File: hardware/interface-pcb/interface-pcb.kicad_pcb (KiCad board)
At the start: 2 copper layers, 100 x 80 mm, 101 parts, among them J1 Siedle bus Ta/Tb, J2 ext. 5V, Q1 IRFR120N, Q2 BC846B, Q3 BCP56-16, Q4 BCP56-16, Q5 BC846B, SW1 setup, U1 R-78CK5.0-0.5, U2 LM393, U3 ES8311, U4 MCP6002, U5 ESP32 D1 Mini

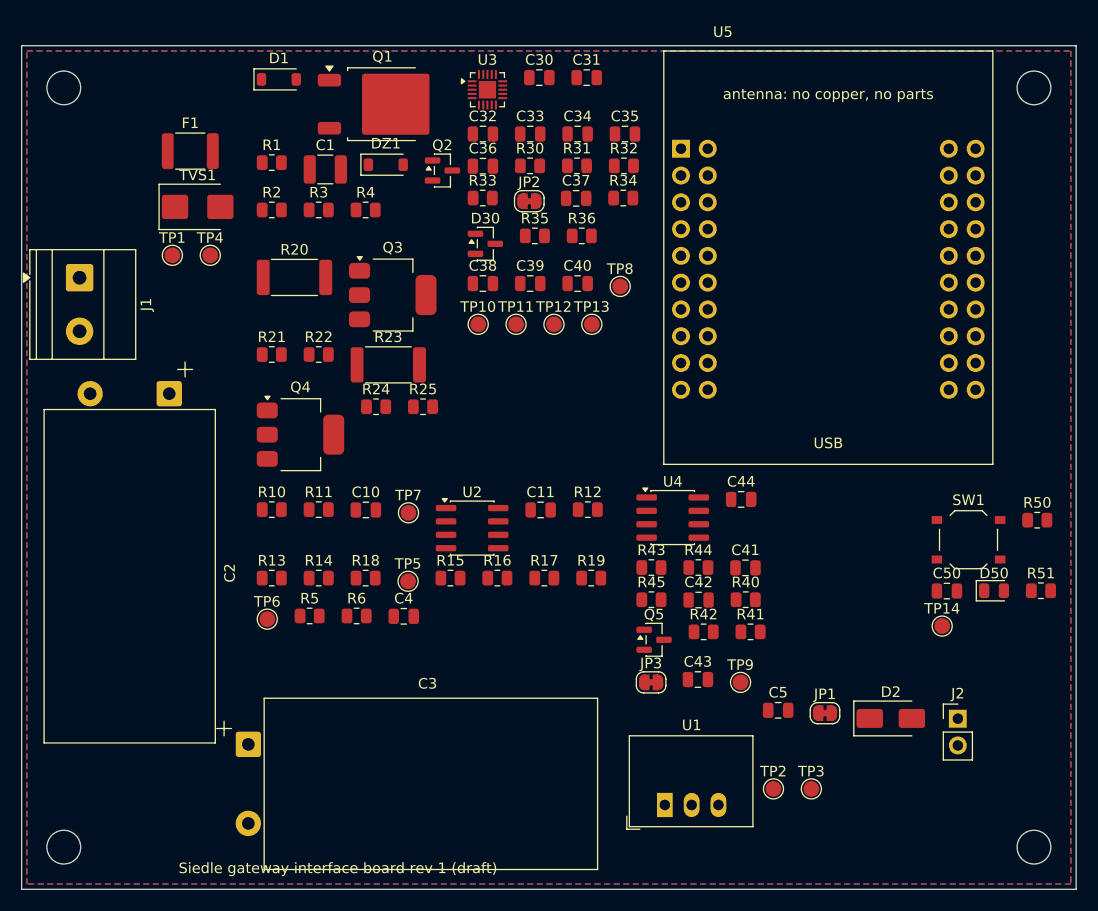
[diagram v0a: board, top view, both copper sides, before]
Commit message: Route the interface board
Routed with Codex: local Freerouting passes, then corrections in
KiCad. The board shrinks to 90 x 75 mm. Audio moves to the lower
middle, away from the antenna and the regulator, which moves to the
right edge.

- Power nets 0.5 mm, pull-down collectors 0.6-0.8 mm, a copper area
  on Q1's drain for the startup heat.
- GND pours on both layers with 63 stitching vias; the ES8311's
  exposed pad reaches its ground pins through short necks, with a
  local 0.15 mm clearance rule for its corner pads
  (interface-pcb.kicad_dru). The board-wide rules get stricter.
- New net classes Ground and Codec; the socket 3D models now sit on
  their pad rows (KiCad's 2 x 10 socket has pin 2 at -2.54 mm).

DRC with refilled zones: no violations, no unconnected items, no
schematic parity issues. PCB.md gets the dimensions for the case.
AGENTS.md records the KiCad scripting pitfalls on macOS, and
tools/kicad-python wraps KiCad's Python with a log.

Co-Authored-By: Claude Opus 5.5 <noreply@anthropic.com>
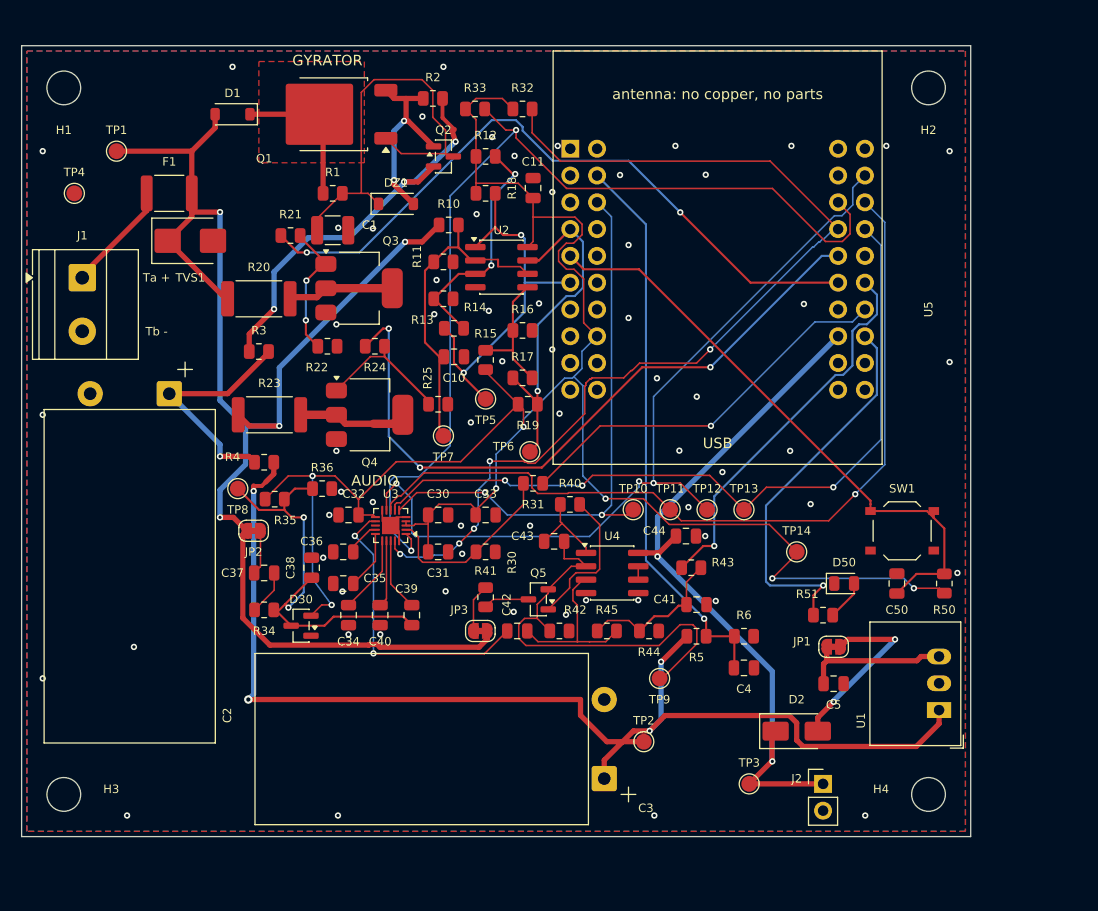
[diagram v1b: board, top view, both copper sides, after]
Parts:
- moved R34 51.8 mm to (73.0, 103.5)
- moved C34 50.5 mm to (81.0, 104.0), turned to -90 degrees
- moved C35 50.3 mm to (80.5, 101.0), turned to 180 degrees
- moved C31 47.1 mm to (89.5, 98.0)
- moved C37 46.2 mm to (73.0, 100.0)
- moved C30 42.6 mm to (89.5, 94.5)
- moved U3 42.3 mm to (85.0, 95.5), turned to 180 degrees
- moved TP8 41.0 mm to (70.5, 92.0)
- moved JP2 40.7 mm to (72.0, 96.0)
- moved D30 40.2 mm to (76.5, 105.0), turned to 180 degrees
- moved C36 38.9 mm to (80.5, 98.0), turned to 180 degrees
- moved C32 38.3 mm to (81.0, 94.5), turned to 180 degrees
- moved R18 38.2 mm to (94.0, 64.0)
- moved R30 36.8 mm to (94.0, 98.0)
- moved R6 36.8 mm to (118.5, 106.0)
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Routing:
- net +3V3: track 0.00 -> 185.0 mm, vias 0 -> 7
- net BUS: track 0.00 -> 133.8 mm, vias 0 -> 4
- net /Bus input and power/VOUT: track 0.00 -> 114.1 mm, vias 0 -> 4
- net I2C_SDA: track 0.00 -> 95.7 mm, vias 0 -> 5
- net I2C_SCL: track 0.00 -> 92.9 mm, vias 0 -> 2
- net I2S_WS: track 0.00 -> 79.1 mm, vias 0 -> 1
- net I2S_DOUT: track 0.00 -> 77.9 mm, vias 0 -> 3
- net I2S_DIN: track 0.00 -> 72.9 mm, vias 0 -> 3
- net +5V: track 0.00 -> 69.6 mm, vias 0 -> 2
- net TX_CARRIER: track 0.00 -> 65.3 mm, vias 0 -> 2
- net TX_BIT: track 0.00 -> 65.3 mm, vias 0 -> 3
- net /BUTTON: track 0.00 -> 57.0 mm
- net I2S_BCLK: track 0.00 -> 54.6 mm, vias 0 -> 2
- net VMON: track 0.00 -> 53.7 mm, vias 0 -> 1
- net /Audio/TX_FB: track 0.00 -> 41.2 mm
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- added copper zone on F.Cu, net /Bus input and power/GYR_D
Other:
- board size 100 x 80 mm -> 90 x 75 mm
- board text added: "AUDIO"
- board text added: "GYRATOR"
- board text added: "SIEDLE GATEWAY / REV 1 DRAFT"
- board text added: "Ta +"
- board text added: "Tb -"
- board text removed: "Siedle gateway interface board rev 1 (draft)"

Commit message: Name the MIC1N net
The redraw wired MIC1N directly, so the Codec net class matched it by
KiCad's pin-derived name, Net-(U3-MIC1N), which changes when U3 or
its pins are renumbered. A label makes it /Audio/MIC1N in the
schematic, the board and the net class pattern.

Co-Authored-By: Claude Opus 5.5 <noreply@anthropic.com>
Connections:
- net Net-(U3-MIC1N) renamed /Audio/MIC1N
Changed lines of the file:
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@@
 			(layers "F.Cu" "F.Mask" "F.Paste")
 			(roundrect_rratio 0.25)
-			(net "Net-(U3-MIC1N)")
+			(net "/Audio/MIC1N")
 		)
 		(pad "2" smd roundrect
@@
 			(layers "F.Cu" "F.Mask" "F.Paste")
 			(roundrect_rratio 0.25)
-			(net "Net-(U3-MIC1N)")
+			(net "/Audio/MIC1N")
 		)
 		(pad "18" smd roundrect
@@
 		(width 0.15)
 		(layer "F.Cu")
-		(net "Net-(U3-MIC1N)")
+		(net "/Audio/MIC1N")
 	)
 	(segment
@@
 		(width 0.15)
 		(layer "F.Cu")
-		(net "Net-(U3-MIC1N)")
+		(net "/Audio/MIC1N")
 	)
 	(segment

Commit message: Decouple U1's input next to its pins
The routing moved U1 to the right edge, away from the codec, which
leaves it about 32 mm from C3, its only input capacitor. A switching
regulator wants the pulsed input current supplied right at its pins,
not through a long track.

C6, a 2.2 uF / 100 V X7R in 1210, sits under the VOUT track a few
millimetres from U1's VIN, with a ground via at its GND pad. It is the
same part as C1 (C153036), so JLCPCB adds no loading fee.

Co-Authored-By: Claude Opus 5.5 <noreply@anthropic.com>
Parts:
- added C6: 2.2u 100V, Capacitor_SMD:C_1210_3225Metric, F.Cu at (130.1, 118.9)
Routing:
- net /Bus input and power/VOUT: track 114.1 -> 116.5 mm
- net GND: track 2.95 -> 5.15 mm, vias 63 -> 64
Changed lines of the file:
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@@
 		)
 	)
+	(footprint "Capacitor_SMD:C_1210_3225Metric"
+		(layer "F.Cu")
+		(at 130.1 118.9 180)
+		(descr "Capacitor SMD 1210 (3225 Metric), square (rectangular) end terminal, IPC-7351 nominal, (Body size source: IPC-SM-782 page 76, https://www.pcb-3d.com/wordpress/wp-content/uploads/ipc-sm-782a_amendment_1_and_2.pdf)")
+		(tags "capacitor")
+		(property "Reference" "C6"
+			(at 0 -2.3 180)
+			(layer "F.SilkS")
+			(effects
+				(font
+					(size 1 1)
+					(thickness 0.15)
+				)
+			)
+		)
+		(property "Value" "2.2u 100V"
+			(at 0 2.3 180)
+			(layer "F.Fab")
+			(effects
+				(font
+					(size 1 1)
+					(thickness 0.15)
+				)
+			)
+		)
+		(property "Datasheet" ""
+			(at 0 0 180)
+			(layer "F.Fab")
+			(hide yes)
+			(effects
+				(font
+					(size 1.27 1.27)
+				)
+			)
+		)
+		(property "Description" "Unpolarized capacitor"
+			(at 0 0 180)
+			(layer "F.Fab")
+			(hide yes)
+			(effects
+				(font
+					(size 1.27 1.27)
+				)
+			)
+		)
+		(property "KiLib_Generator" "SMD_2terminal_chip_molded"
+			(at 0 0 180)
+			(layer "F.SilkS")
+			(hide yes)
+			(effects
+				(font
+					(size 1 1)
+					(thickness 0.15)
+				)
+			)
+		)
+		(property "LCSC" "C153036"
+			(at 0 0 180)
+			(layer "F.SilkS")
+			(hide yes)
+			(effects
+				(font
+					(size 1.27 1.27)
+					(thickness 0.15)
+				)
+			)
+		)
+		(property "Note" "U1 input, next to its pins; same part as C1"
+			(at 0 0 180)
+			(layer "F.SilkS")
+			(hide yes)
+			(effects
+				(font
+					(size 1.27 1.27)
+					(thickness 0.15)
+				)
+			)
+		)
+		(sheetname "Bus input and power")
+		(sheetfile "bus_power.kicad_sch")
+		(attr smd)
+		(duplicate_pad_numbers_are_jumpers no)
+		(fp_line
+			(start -0.711252 1.36)
+			(end 0.711252 1.36)
+			(stroke
+				(width 0.12)
+				(type solid)
+			)
+			(layer "F.SilkS")
+		)
+		(fp_line
+			(start -0.711252 -1.36)
+			(end 0.711252 -1.36)
+			(stroke
+				(width 0.12)
+				(type solid)
+			)
+			(layer "F.SilkS")
+		)
+		(fp_rect
+			(start -2.3 -1.6)
+			(end 2.3 1.6)
+			(stroke
+				(width 0.05)
+				(type solid)
+			)
+			(fill no)
+			(layer "F.CrtYd")
+		)
+		(fp_rect
+			(start -1.6 -1.25)
+			(end 1.6 1.25)
+			(stroke
+				(width 0.1)
+				(type solid)
+			)
+			(fill no)
+			(layer "F.Fab")
+		)
+		(fp_text user "${REFERENCE}"
+			(at 0 0 180)
+			(layer "F.Fab")
+			(effects
+				(font
+					(size 0.8 0.8)
+					(thickness 0.12)
+				)
+			)
+		)
+		(pad "1" smd roundrect
+			(at -1.475 0 180)
+			(size 1.15 2.7)
+			(layers "F.Cu" "F.Mask" "F.Paste")
+			(roundrect_rratio 0.217391)
+			(net "/Bus input and power/VOUT")
+		)
+		(pad "2" smd roundrect
+			(at 1.475 0 180)
+			(size 1.15 2.7)
+			(layers "F.Cu" "F.Mask" "F.Paste")
+			(roundrect_rratio 0.217391)
+			(net "GND")
+		)
+		(embedded_fonts no)
+		(model "${KICAD10_3DMODEL_DIR}/Capacitor_SMD.3dshapes/C_1210_3225Metric.step"
+			(offset
+				(xyz 0 0 0)
+			)
+			(scale
+				(xyz 1 1 1)
+			)
+			(rotate
+				(xyz 0 0 0)
+			)
+		)
+	)
 	(footprint "gateway:D1_Mini_ESP32_Socket"
 		(layer "F.Cu")
@@
 		(tags "mountinghole M3")
 		(property "Reference" "H4"
-			(at -4.5 -0.5 0)
+			(at -4.5 2.6 0)
 			(layer "F.SilkS")
 			(effects
@@
 		(net "GND")
 	)
+	(segment
+		(start 128.625 118.9)
+		(end 128.625 121.1)
+		(width 0.5)
+		(layer "F.Cu")
+		(net "GND")
+	)
 	(via
 		(at 112 59.5)
@@
 	)
 	(via
+		(at 128.625 121.1)
+		(size 0.6)
+		(drill 0.3)
+		(layers "F.Cu" "B.Cu")
+		(net "GND")
+	)
+	(via
 		(at 138.7405 100)
 		(size 0.6)
@@
 		(width 0.5)
 		(layer "F.Cu")
+		(net "/Bus input and power/VOUT")
+	)
+	(segment
+		(start 131.575 118.9)
+		(end 131.575 116.48)
+		(width 0.5)
+		(layer "F.Cu")
